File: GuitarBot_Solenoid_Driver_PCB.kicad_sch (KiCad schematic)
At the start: 46 parts, among them J1 Screw_Terminal_01x02, J2 Screw_Terminal_01x16, J3 Screw_Terminal_01x16, J4 Screw_Terminal_01x04, Q1 NMOS, Q10 NMOS, Q11 NMOS, Q12 NMOS, Q13 NMOS, Q14 NMOS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

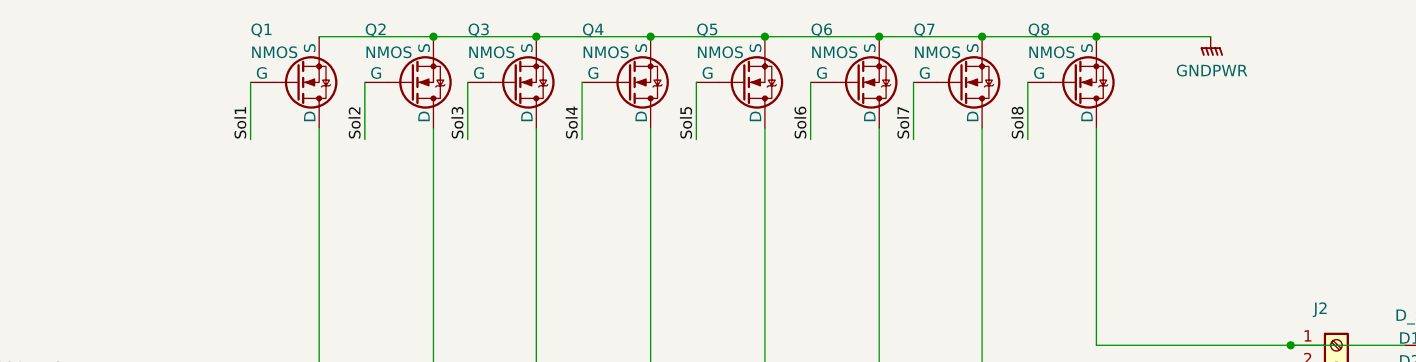
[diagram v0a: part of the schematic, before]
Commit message: Started pcb layout and updated schematic
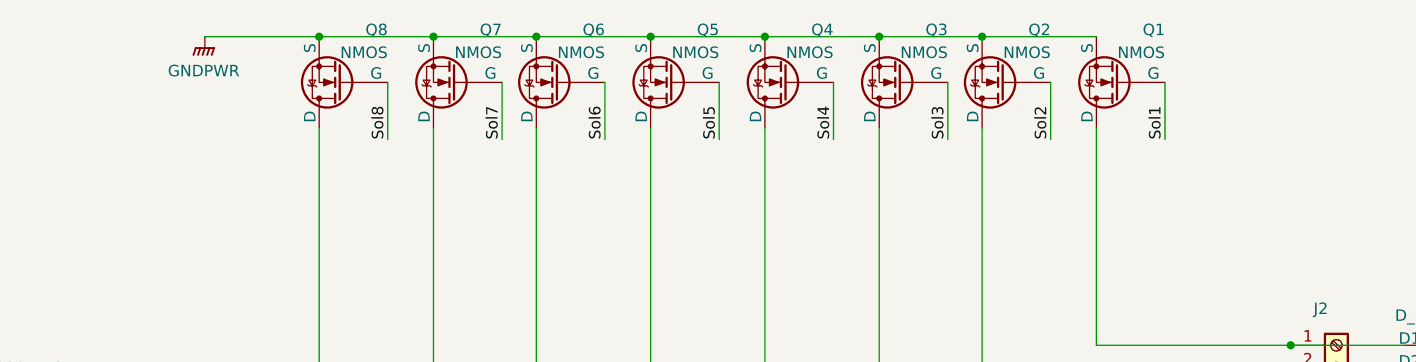
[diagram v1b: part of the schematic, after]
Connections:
- net at D6.2 (A), J2.6 (Pin_6): now also Q6.1 (D); no longer Q3.1 (D)
- net at D2.2 (A), J2.2 (Pin_2): now also Q2.1 (D); no longer Q7.1 (D)
- net at D7.2 (A), J2.7 (Pin_7): now also Q7.1 (D); no longer Q2.1 (D)
- net at D3.2 (A), J2.3 (Pin_3): now also Q3.1 (D); no longer Q6.1 (D)
- net at D8.2 (A), J2.8 (Pin_8): now also Q8.1 (D); no longer Q1.1 (D)
- net at D1.2 (A), J2.1 (Pin_1): now also Q1.1 (D); no longer Q8.1 (D)
- net at D4.2 (A), J2.4 (Pin_4): now also Q4.1 (D); no longer Q5.1 (D)
- net at D5.2 (A), J2.5 (Pin_5): now also Q5.1 (D); no longer Q4.1 (D)
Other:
- moved on the sheet: Q1, Q2, Q3, Q4, Q5, Q6, Q7, Q8
